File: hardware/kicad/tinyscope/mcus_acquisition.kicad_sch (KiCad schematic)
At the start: 30 parts, among them J5 STM32H743, Q2 NMOS, SW1 SW_SPST, U12 STM32H743VITx, X1 25MHz, X2 32k768

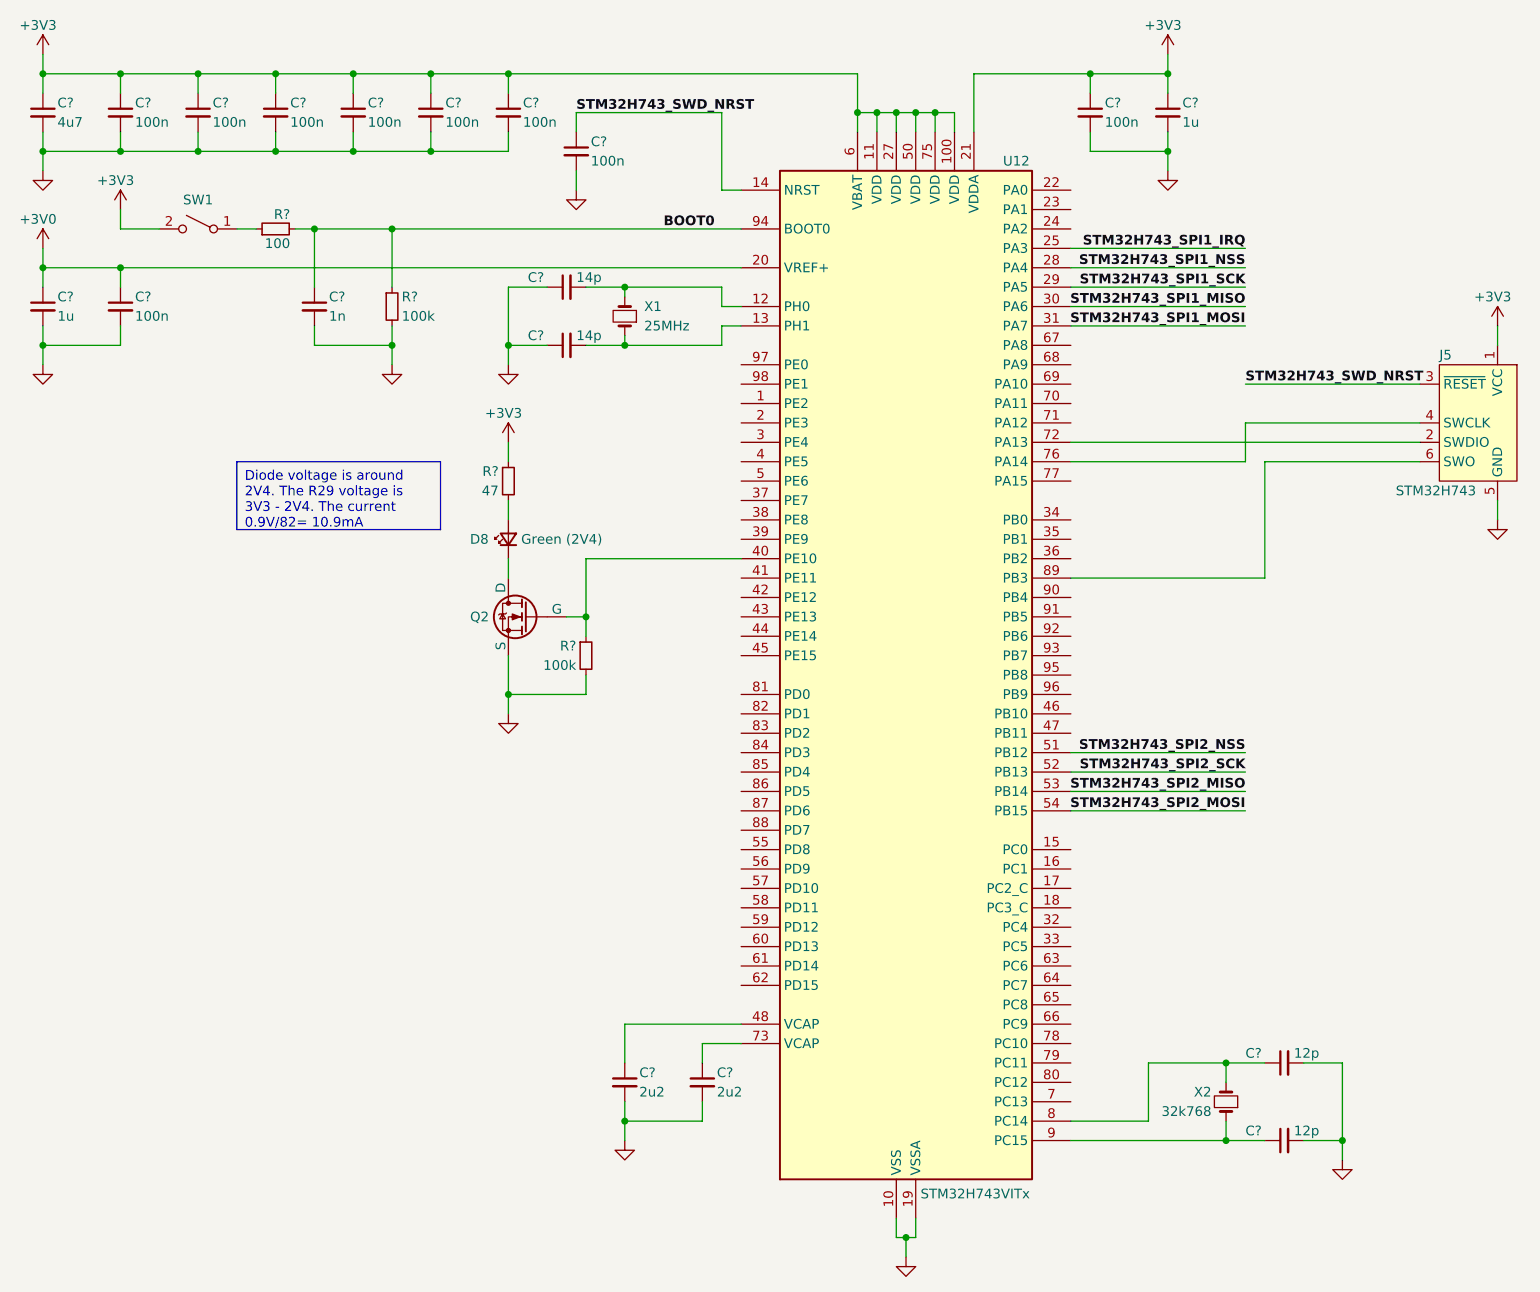
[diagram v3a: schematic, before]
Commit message: feat: hardware: Adds five encoders inputs on STM32H743
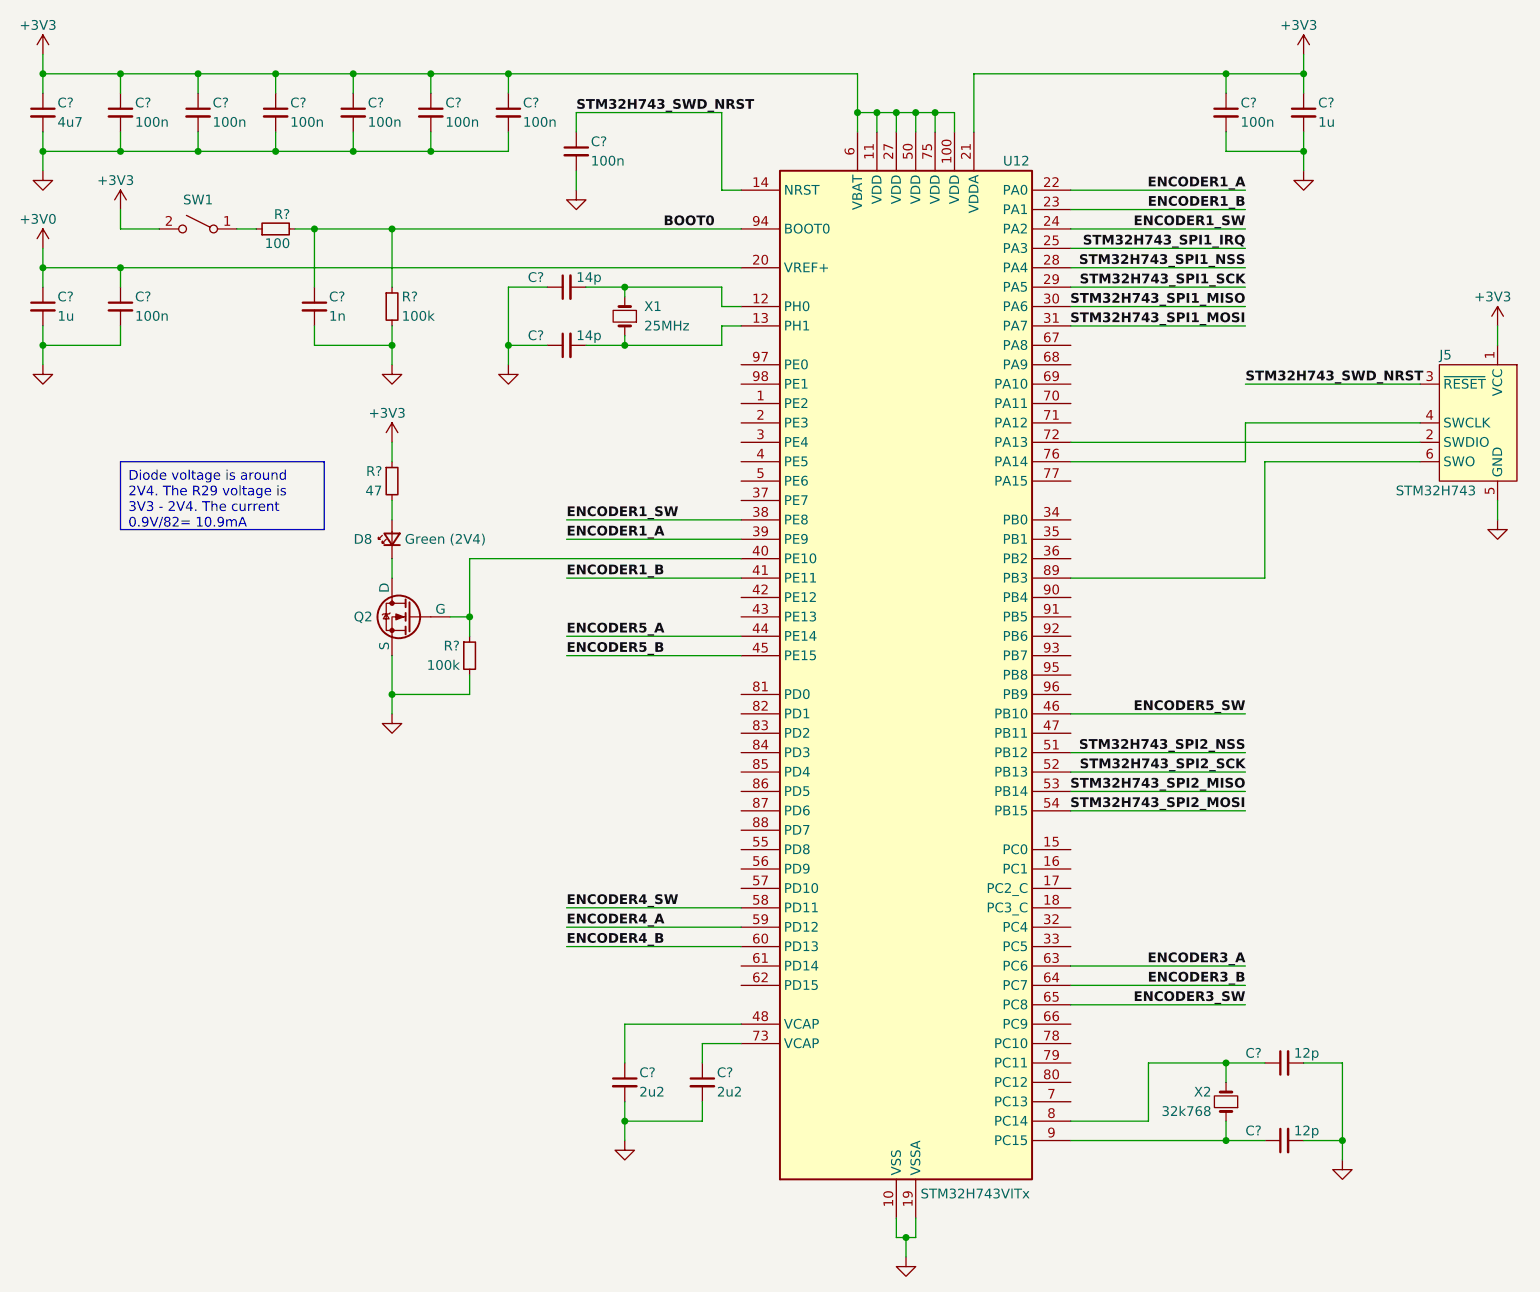
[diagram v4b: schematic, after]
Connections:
- net ENCODER1_A: now reaches U12.22 (PA0)
- net ENCODER1_A: now also U12.39 (PE9)
- net ENCODER1_B: now reaches U12.23 (PA1)
- net ENCODER1_B: now also U12.41 (PE11)
- net ENCODER1_SW: now reaches U12.24 (PA2)
- net ENCODER1_SW: now also U12.38 (PE8)
- net ENCODER5_A: now reaches U12.44 (PE14)
- net ENCODER5_B: now reaches U12.45 (PE15)
- net ENCODER5_SW: now reaches U12.46 (PB10)
- net ENCODER4_SW: now reaches U12.58 (PD11)
- net ENCODER4_A: now reaches U12.59 (PD12)
- net ENCODER4_B: now reaches U12.60 (PD13)
- net ENCODER3_A: now reaches U12.63 (PC6)
- net ENCODER3_B: now reaches U12.64 (PC7)
- net ENCODER3_SW: now reaches U12.65 (PC8)
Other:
- moved on the sheet: C?, D8, Q2, R?

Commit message: feat: hardware: Connects all five encoders to STM32H743
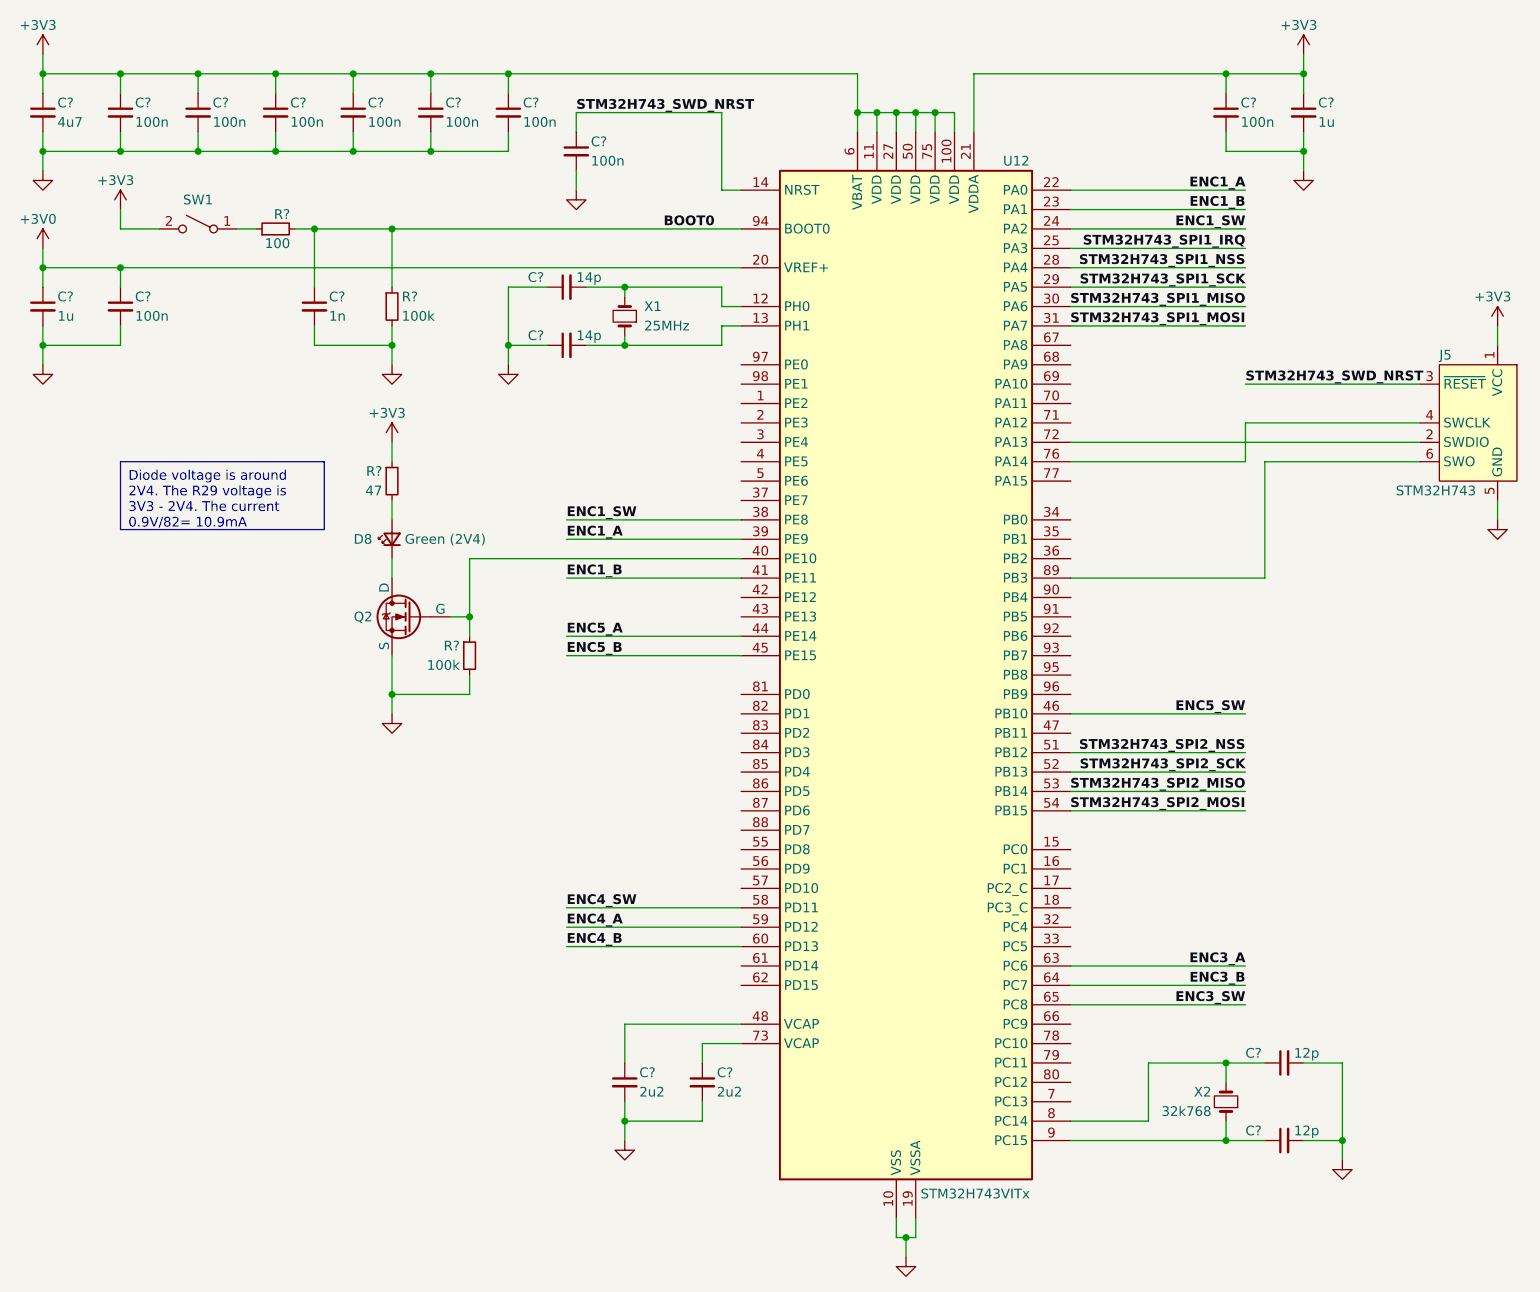
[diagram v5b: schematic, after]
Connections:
- net ENCODER1_A renamed ENC1_A
- net ENCODER1_B renamed ENC1_B
- net ENCODER1_SW renamed ENC1_SW
- net ENCODER3_A renamed ENC3_A
- net ENCODER3_B renamed ENC3_B
- net ENCODER3_SW renamed ENC3_SW
- net ENCODER4_A renamed ENC4_A
- net ENCODER4_B renamed ENC4_B
- net ENCODER4_SW renamed ENC4_SW
- net ENCODER5_A renamed ENC5_A
- net ENCODER5_B renamed ENC5_B
- net ENCODER5_SW renamed ENC5_SW
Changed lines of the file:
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@@
     (effects (font (size 1.27 1.27) bold) (justify left bottom))
   )
-  (label "ENCODER1_A" (at 200.66 35.56 180) (fields_autoplaced)
+  (label "ENC1_A" (at 200.66 35.56 180) (fields_autoplaced)
     (effects (font (size 1.27 1.27) bold) (justify right bottom))
   )
@@
     (effects (font (size 1.27 1.27) bold) (justify right bottom))
   )
-  (label "ENCODER1_SW" (at 111.76 78.74 0) (fields_autoplaced)
+  (label "ENC1_SW" (at 111.76 78.74 0) (fields_autoplaced)
     (effects (font (size 1.27 1.27) bold) (justify left bottom))
   )
@@
     (effects (font (size 1.27 1.27) bold) (justify right bottom))
   )
-  (label "ENCODER1_SW" (at 200.66 40.64 180) (fields_autoplaced)
+  (label "ENC1_SW" (at 200.66 40.64 180) (fields_autoplaced)
     (effects (font (size 1.27 1.27) bold) (justify right bottom))
   )
@@
     (effects (font (size 1.27 1.27) bold) (justify left bottom))
   )
-  (label "ENCODER3_A" (at 200.66 137.16 180) (fields_autoplaced)
+  (label "ENC3_A" (at 200.66 137.16 180) (fields_autoplaced)
     (effects (font (size 1.27 1.27) bold) (justify right bottom))
   )
-  (label "ENCODER5_SW" (at 200.66 104.14 180) (fields_autoplaced)
+  (label "ENC5_SW" (at 200.66 104.14 180) (fields_autoplaced)
     (effects (font (size 1.27 1.27) bold) (justify right bottom))
   )
-  (label "ENCODER3_B" (at 200.66 139.7 180) (fields_autoplaced)
+  (label "ENC3_B" (at 200.66 139.7 180) (fields_autoplaced)
     (effects (font (size 1.27 1.27) bold) (justify right bottom))
   )
@@
     (effects (font (size 1.27 1.27) bold) (justify left bottom))
   )
-  (label "ENCODER3_SW" (at 200.66 142.24 180) (fields_autoplaced)
+  (label "ENC3_SW" (at 200.66 142.24 180) (fields_autoplaced)
     (effects (font (size 1.27 1.27) bold) (justify right bottom))
   )
@@
     (effects (font (size 1.27 1.27) bold) (justify right bottom))
   )
-  (label "ENCODER1_B" (at 200.66 38.1 180) (fields_autoplaced)
+  (label "ENC1_B" (at 200.66 38.1 180) (fields_autoplaced)
     (effects (font (size 1.27 1.27) bold) (justify right bottom))
   )
@@
     (effects (font (size 1.27 1.27) bold) (justify right bottom))
   )
-  (label "ENCODER4_B" (at 111.76 134.62 0) (fields_autoplaced)
+  (label "ENC4_B" (at 111.76 134.62 0) (fields_autoplaced)
     (effects (font (size 1.27 1.27) bold) (justify left bottom))
   )
@@
     (effects (font (size 1.27 1.27) bold) (justify right bottom))
   )
-  (label "ENCODER4_SW" (at 111.76 129.54 0) (fields_autoplaced)
+  (label "ENC4_SW" (at 111.76 129.54 0) (fields_autoplaced)
     (effects (font (size 1.27 1.27) bold) (justify left bottom))
   )
-  (label "ENCODER5_B" (at 111.76 96.52 0) (fields_autoplaced)
+  (label "ENC5_B" (at 111.76 96.52 0) (fields_autoplaced)
     (effects (font (size 1.27 1.27) bold) (justify left bottom))
   )
-  (label "ENCODER1_B" (at 111.76 86.36 0) (fields_autoplaced)
+  (label "ENC1_B" (at 111.76 86.36 0) (fields_autoplaced)
     (effects (font (size 1.27 1.27) bold) (justify left bottom))
   )
-  (label "ENCODER1_A" (at 111.76 81.28 0) (fields_autoplaced)
+  (label "ENC1_A" (at 111.76 81.28 0) (fields_autoplaced)
     (effects (font (size 1.27 1.27) bold) (justify left bottom))
   )
@@
     (effects (font (size 1.27 1.27) bold) (justify right bottom))
   )
-  (label "ENCODER5_A" (at 111.76 93.98 0) (fields_autoplaced)
+  (label "ENC5_A" (at 111.76 93.98 0) (fields_autoplaced)
     (effects (font (size 1.27 1.27) bold) (justify left bottom))
   )
-  (label "ENCODER4_A" (at 111.76 132.08 0) (fields_autoplaced)
+  (label "ENC4_A" (at 111.76 132.08 0) (fields_autoplaced)
     (effects (font (size 1.27 1.27) bold) (justify left bottom))
   )
